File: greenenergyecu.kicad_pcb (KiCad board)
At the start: 2 copper layers, 34.5 x 20.5 mm, 1 part, among them U1 ICM7555xB

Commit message: yhd
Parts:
- added U2: ICM7555xB, Package_SO:SOIC-8_3.9x4.9mm_P1.27mm, F.Cu at (8.53, 6.59)
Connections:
- U1 pad 3: unconnected-(U1-Q-Pad3) -> Net-(U1-Q)
- U1 pad 7: unconnected-(U1-DIS-Pad7) -> Net-(U1-DIS)
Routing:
- net Net-(U1-DIS): track 0.00 -> 21.2 mm
- net Net-(U1-Q): track 0.00 -> 14.5 mm
- net Net-(U2-TR): track 0.00 -> 12.1 mm

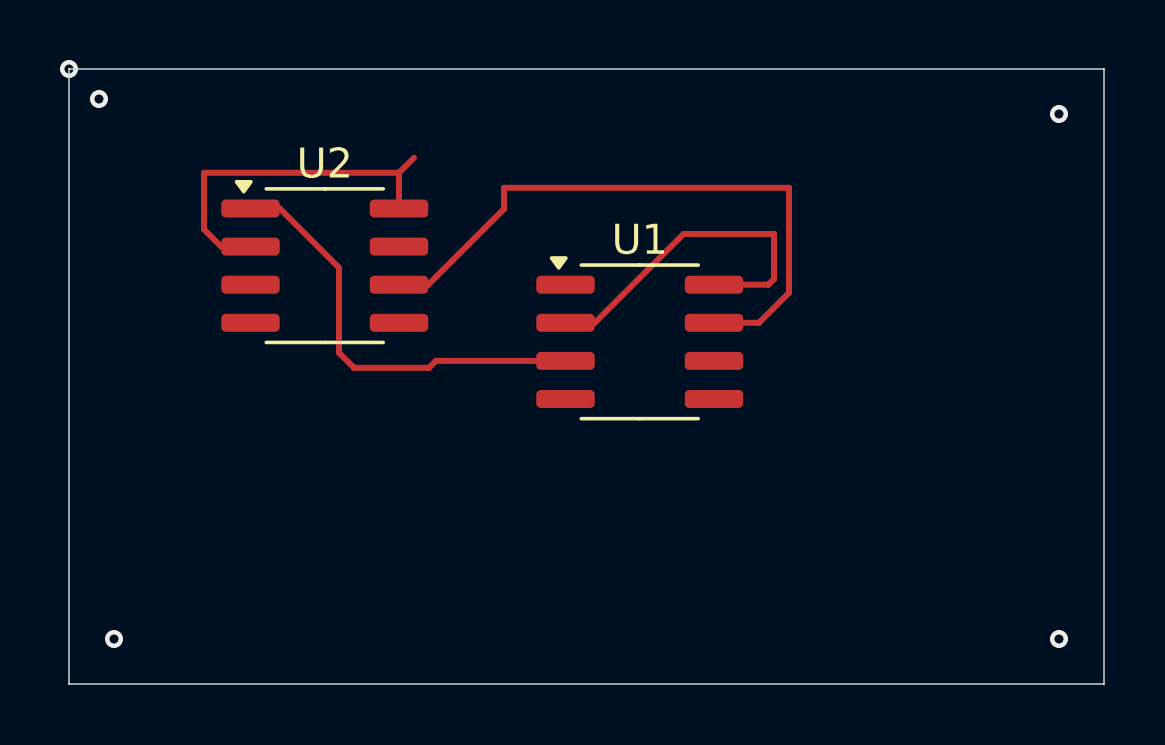
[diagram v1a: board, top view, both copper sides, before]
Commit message: agrege el footpit
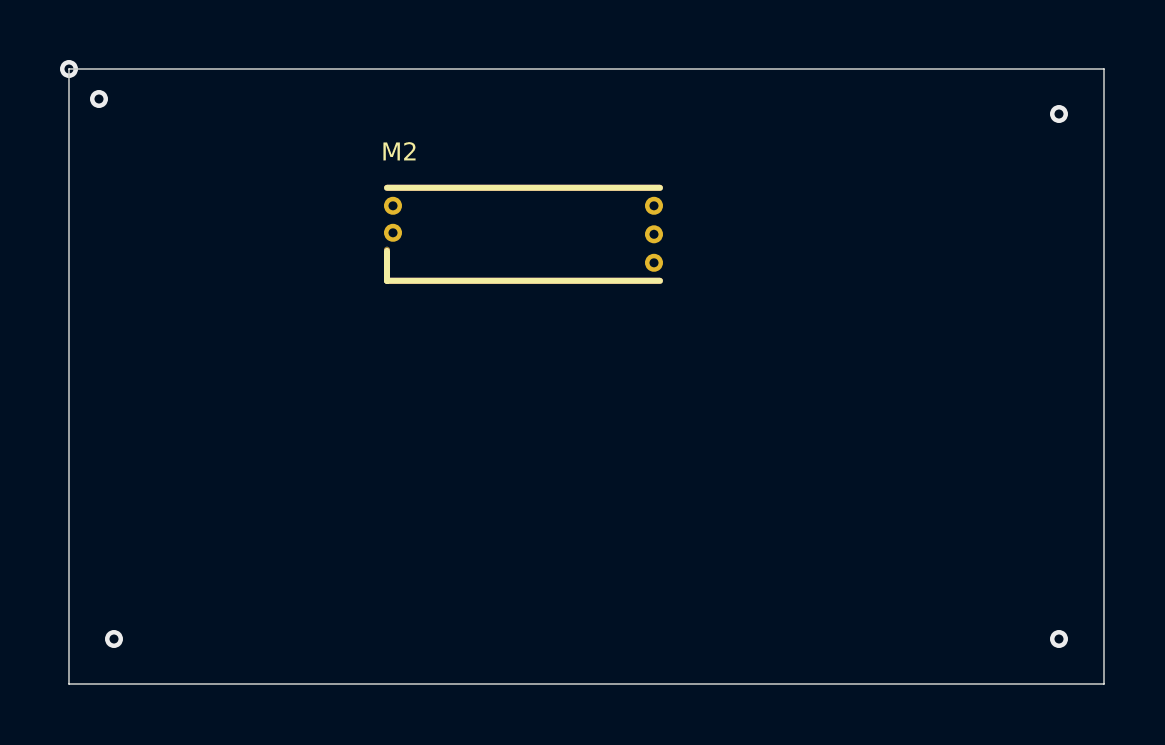
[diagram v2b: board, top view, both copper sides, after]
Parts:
- removed U1, U2: ICM7555xB, Package_SO:SOIC-8_3.9x4.9mm_P1.27mm
- added M2: Module-knock-0.2, hellen-one-knock-0.2:knock, F.Cu at (10.5, 7.20)
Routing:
- net Net-(U1-DIS): track 21.2 -> 0.00 mm
- net Net-(U1-Q): track 14.5 -> 0.00 mm
- net Net-(U2-TR): track 12.1 -> 0.00 mm
- net Net-(U1-TR): track 11.8 -> 0.00 mm
